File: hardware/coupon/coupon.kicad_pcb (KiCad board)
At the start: 4 copper layers, 80 x 60 mm, 78 parts, among them SW1 tactile

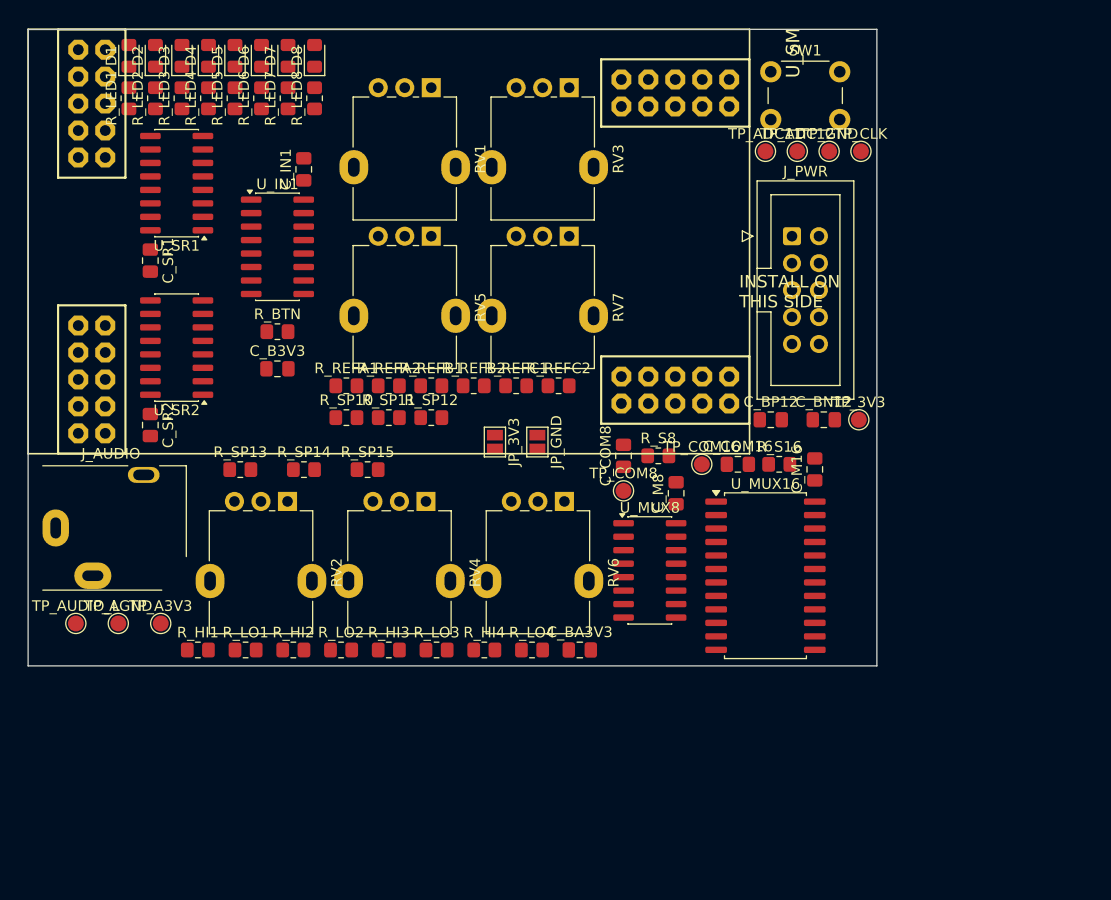
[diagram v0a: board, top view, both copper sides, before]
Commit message: hw(coupon): the board grows to 100x80, and nothing hides under the module
Co-Authored-By: HAL 9000 <293417720+bea-ton-k@users.noreply.github.com>
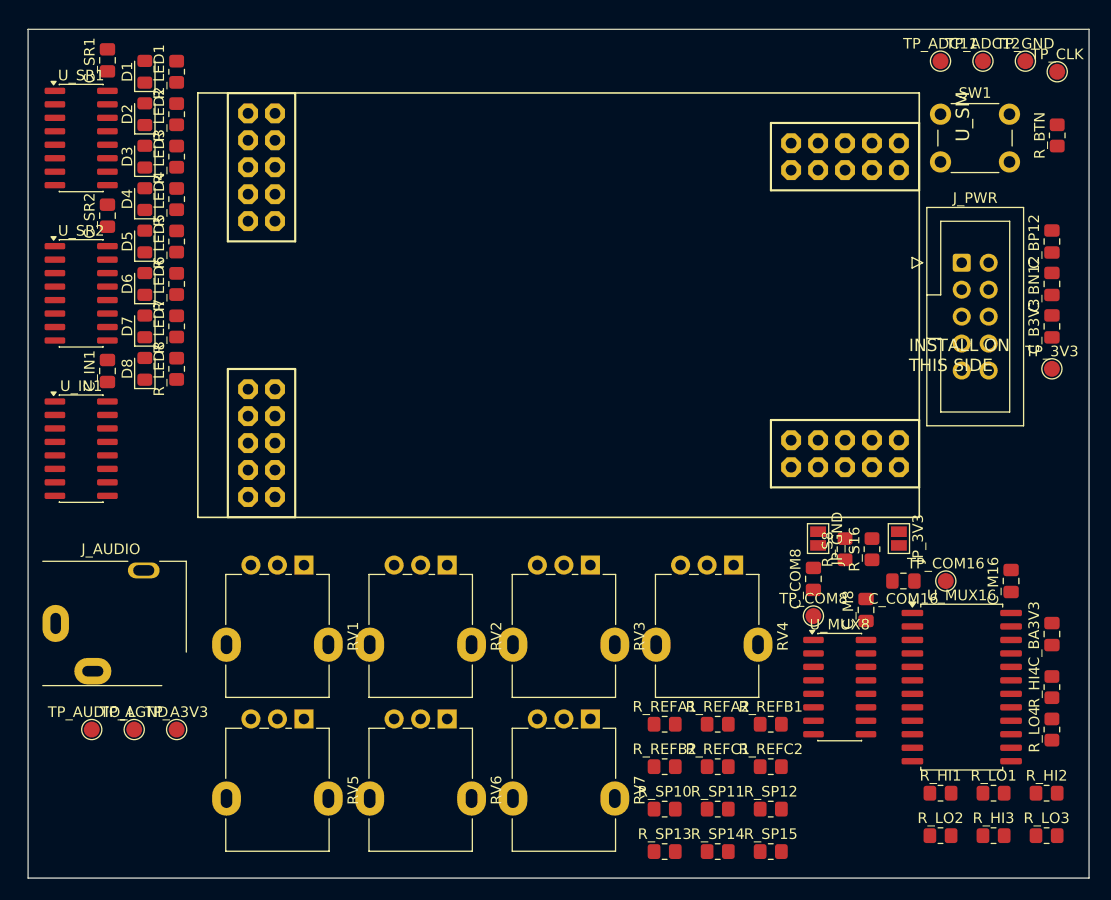
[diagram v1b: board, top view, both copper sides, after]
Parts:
- moved R_BTN 75.8 mm to (97.0, 10.0), turned to 90 degrees
- moved C_B3V3 73.1 mm to (96.5, 28.0), turned to 90 degrees
- moved R_HI2 72.3 mm to (96.0, 72.0)
- moved R_LO1 71.8 mm to (91.0, 72.0)
- moved R_HI1 71.3 mm to (86.0, 72.0)
- moved R_LO3 60.1 mm to (96.0, 76.0)
- moved R_HI3 59.6 mm to (91.0, 76.0)
- moved R_LO2 59.1 mm to (86.0, 76.0)
- moved R_SP13 53.8 mm to (60.0, 77.5)
- moved R_HI4 53.6 mm to (96.5, 62.0), turned to 90 degrees
- moved R_SP14 53.1 mm to (65.0, 77.5)
- moved R_SP15 52.3 mm to (70.0, 77.5)
- moved R_LO4 49.6 mm to (96.5, 66.0), turned to 90 degrees
- moved R_SP12 48.8 mm to (70.0, 73.5)
- moved R_SP11 48.2 mm to (65.0, 73.5)
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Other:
- board size 80 x 60 mm -> 100 x 80 mm

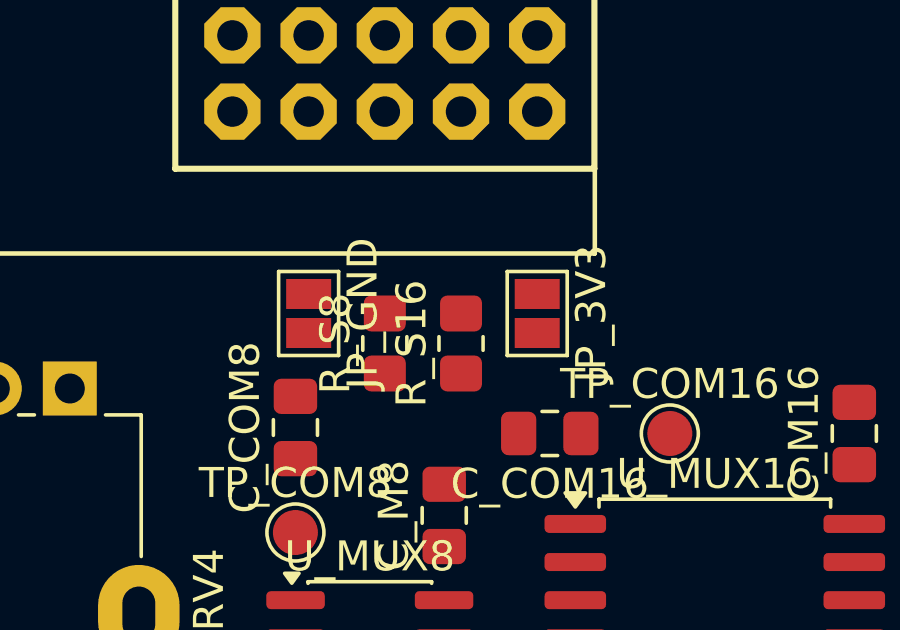
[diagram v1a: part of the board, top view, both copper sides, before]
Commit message: hw(coupon): the courtyard gate learns to fail, and to see the module
Co-Authored-By: HAL 9000 <293417720+bea-ton-k@users.noreply.github.com>
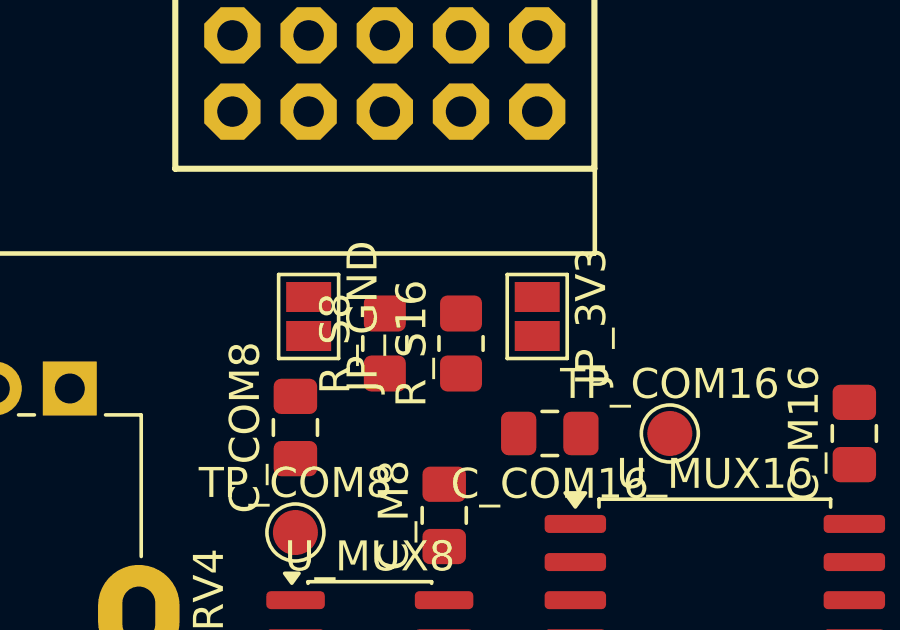
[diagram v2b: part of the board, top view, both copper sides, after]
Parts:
- moved JP_3V3 0.10 mm to (82.1, 48.1)
- moved JP_GND 0.10 mm to (74.5, 48.1)

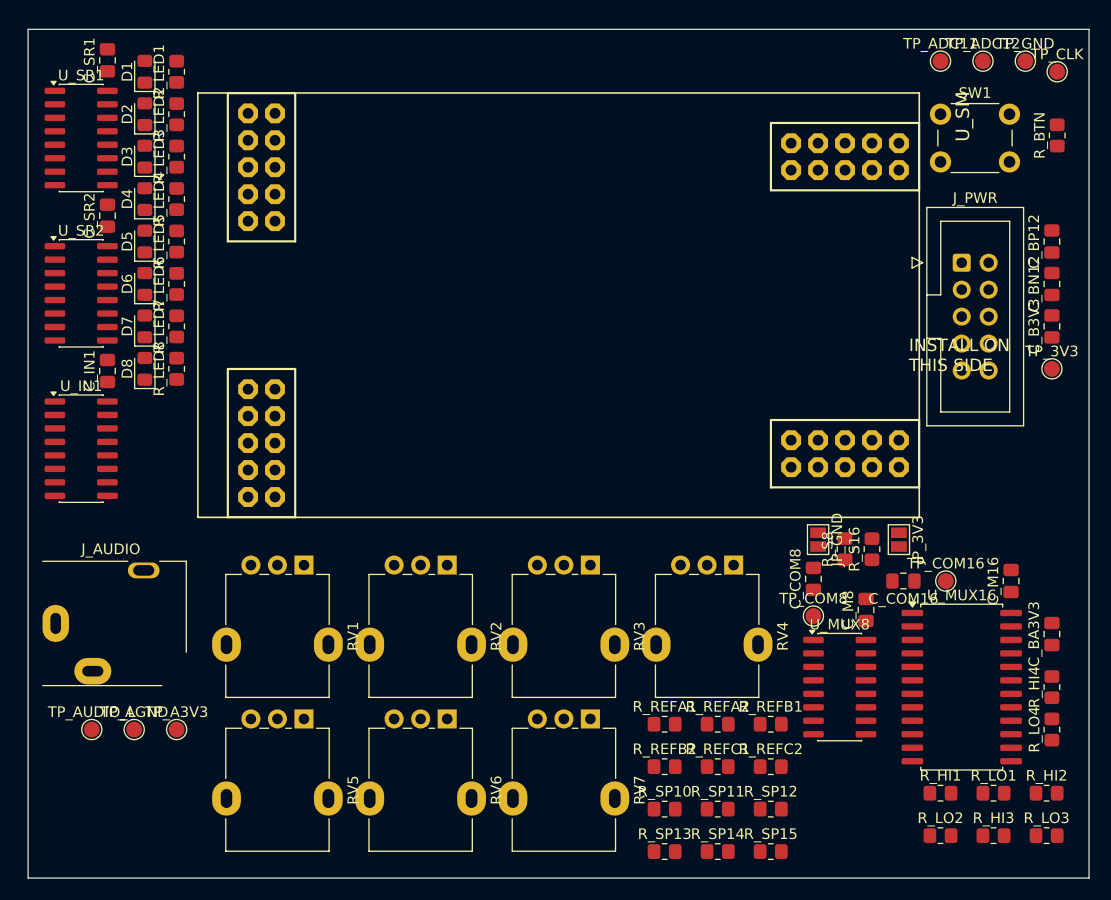
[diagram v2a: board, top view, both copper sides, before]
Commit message: hw(coupon): four split planes, joined only where the jumpers say
Zones from placement.ZONE_RECTS plus one stitching via + 0.5 mm F.Cu track
per SMD pad on a plane net, generated mechanically from the board's own
pads (through-hole plane pads reach In1/In2 through their own holes and
need nothing). Proof step 5 checks every pad on GND/AGND/+3V3/A+3V3 is
actually joined to its plane.

CONNECTIVITY_DATA's Python bindings can't answer that per-net question
directly here (GetNetItems/RunOnUnconnectedEdges both raise TypeError on
the std::vector<KICAD_T>/std::function typemaps; IsConnectedOnLayer answers
a different question and stays False for a pad stitched in one layer away)
-- probed and recorded in build_pcb.py, so the check re-parses kicad-cli's
own DRC report instead, the same trust-kicad-cli choice check_courtyards
already makes for courtyard overlaps.

The via direction took two failed attempts before landing on courtyard-
normalized axis selection: the raw pad-to-footprint-centre vector, and then
raw-magnitude axis snapping, both walked a stitching via on a two-row IC
straight into the neighbouring pin's pad -- a real shorting_items DRC
violation both times. Normalizing each axis by the footprint's own
courtyard half-extent fixed it; zero shorts in the final report.

Co-Authored-By: HAL 9000 <293417720+bea-ton-k@users.noreply.github.com>
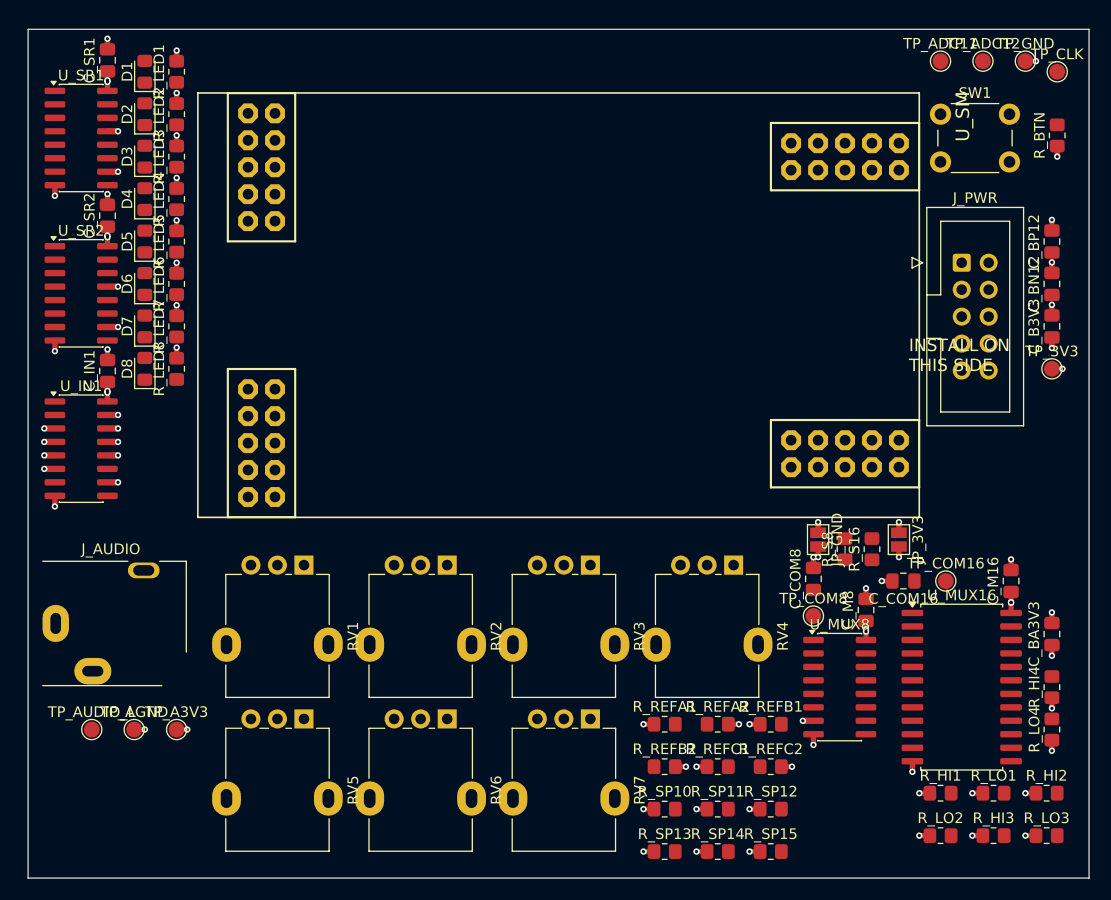
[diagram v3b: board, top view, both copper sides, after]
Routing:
- net GND: track 0.00 -> 30.0 mm, vias 0 -> 30
- net AGND: track 0.00 -> 23.0 mm, vias 0 -> 23
- net A+3V3: track 0.00 -> 14.0 mm, vias 0 -> 14
- net +3V3: track 0.00 -> 12.0 mm, vias 0 -> 12
- added copper zone on In2.Cu, net +3V3
- added copper zone on In2.Cu, net A+3V3
- added copper zone on In1.Cu, net AGND
- added copper zone on In1.Cu, net GND

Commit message: hw(coupon): the stitch search earns its own gate, and stops guessing once
Review round 1: check_courtyards only ever gated courtyards_overlap, so the
"zero shorting_items" the Task-3 report claimed was verified once and
enforced never. Add check_stitch_hygiene as proof step 6, hard-gating
shorting_items/clearance/hole_clearance/hole_to_hole at zero against the
same DRC report -- all four were genuinely zero in the Task-2 baseline, so
this is a real regression boundary. Proved red with a scratchpad-only
perturbation (a GND via dropped 0.05 mm from a +12V pad); no repo file
touched, confirmed by git status immediately after.

Replace the single-guess via placement with _find_via_offset(), a real
collision search: same courtyard-normalized starting direction, then the
perpendicular axis, then both reversed, at growing standoff up to 3.0 mm,
checked against every other-net pad's actual bounding box and every via
already placed this pass. Clears both severe cases review round 1 named
(the C_BP12/C_BN12 +-12V-adjacent via at 0.0375 mm actual clearance, and
the LED-column squeezes at ~0.10-0.15 mm) plus the via-born hole_to_hole
pairs -- all 79 stitched pads resolve on the first search, nothing left to
adjudicate. placement.py untouched; the fix only changes where within its
search radius a via lands.

Co-Authored-By: HAL 9000 <293417720+bea-ton-k@users.noreply.github.com>
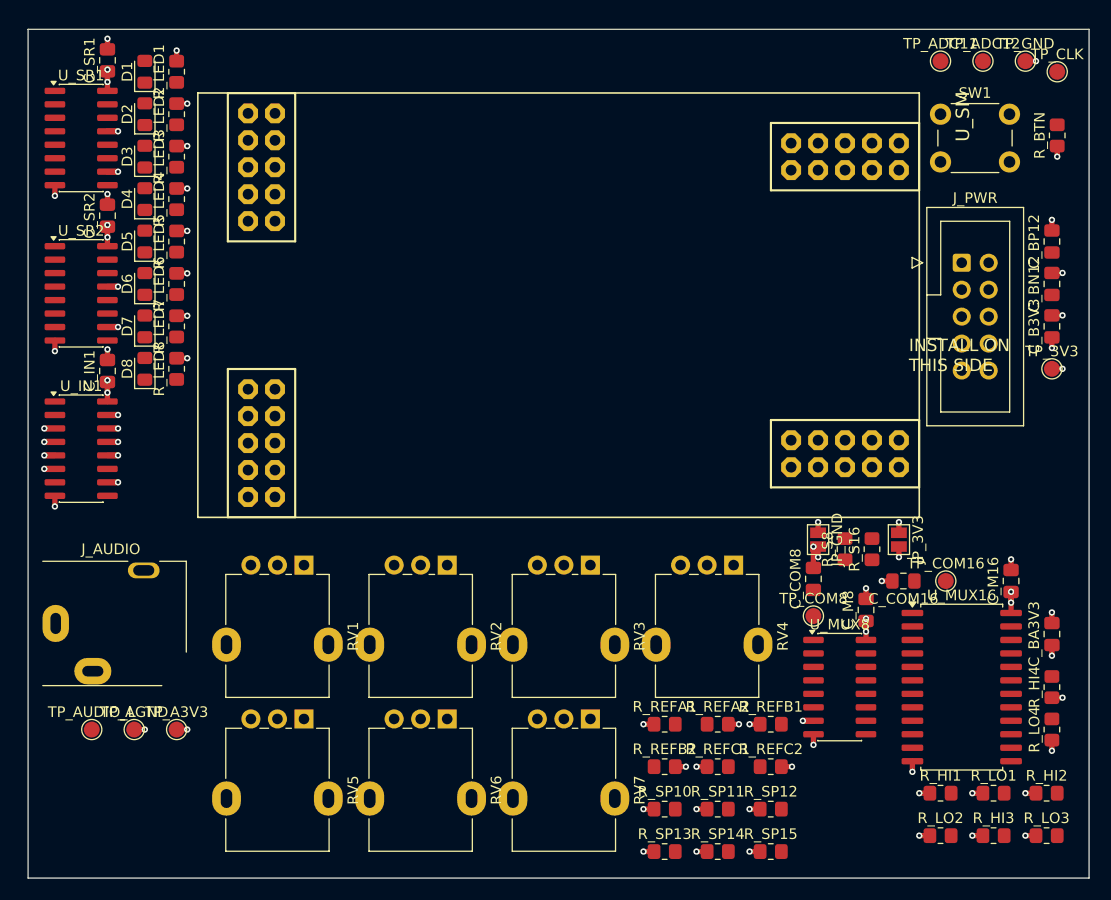
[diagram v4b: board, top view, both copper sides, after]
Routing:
- net +3V3: track 12.0 -> 15.0 mm
- net A+3V3: track 14.0 -> 16.0 mm
- net AGND: track 23.0 -> 24.0 mm

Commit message: hw(coupon): the routing is data, and the ratsnest is down to ten
74 of the board's 84 unconnected pairs are copper now, and every other gate
is green -- including tracks_crossing, which this commit adds to the DRC
classes build_pcb.py refuses to pass. It earned that on the first routing
round: the opening +-12 V draft crossed -12 V over the +12 V lane and step 3
was still filing that class under "not gated here". Fifteen further crossings
turned up behind it, every one a short.

routing.py is data and a resolver, not a router. Endpoints are named
("pad", "U_SM", "A5") and resolved from the built board, so moving a part in
placement.py moves the track's end with it. The corners in between are
hand-placed, and the reasons are written down beside them, because the
numbers that decide this layout are not visible from the source: the module's
landing pads leave 0.66 mm between neighbours against the 0.65 mm a 0.25 mm
track needs, so nothing threads a bank; an SOIC-16 leaves 0.67 mm against the
same 0.65 mm, so seven of the eight LED anodes go under the board; and Task
3's stitching sits at 1.27 mm pitch through every corridor the analog
fan-out wanted.

Ten pairs are still open, all of them the address/enable bus landing at the
two muxes and the 8:1's two east-column ties. The blocker is an ordering
contradiction rather than a shortage of room -- the fan-out order at U_SR1's
via column and the landing order at the 16:1's pins disagree about MUX_A2 and
MUX_A3, and the 16:1's own east-column descents wall the 8:1 off from its two
far ties. Written up in full in the task report; it looks like a placement
question, and placement is not this task's to change.

Co-Authored-By: HAL 9000 <293417720+bea-ton-k@users.noreply.github.com>
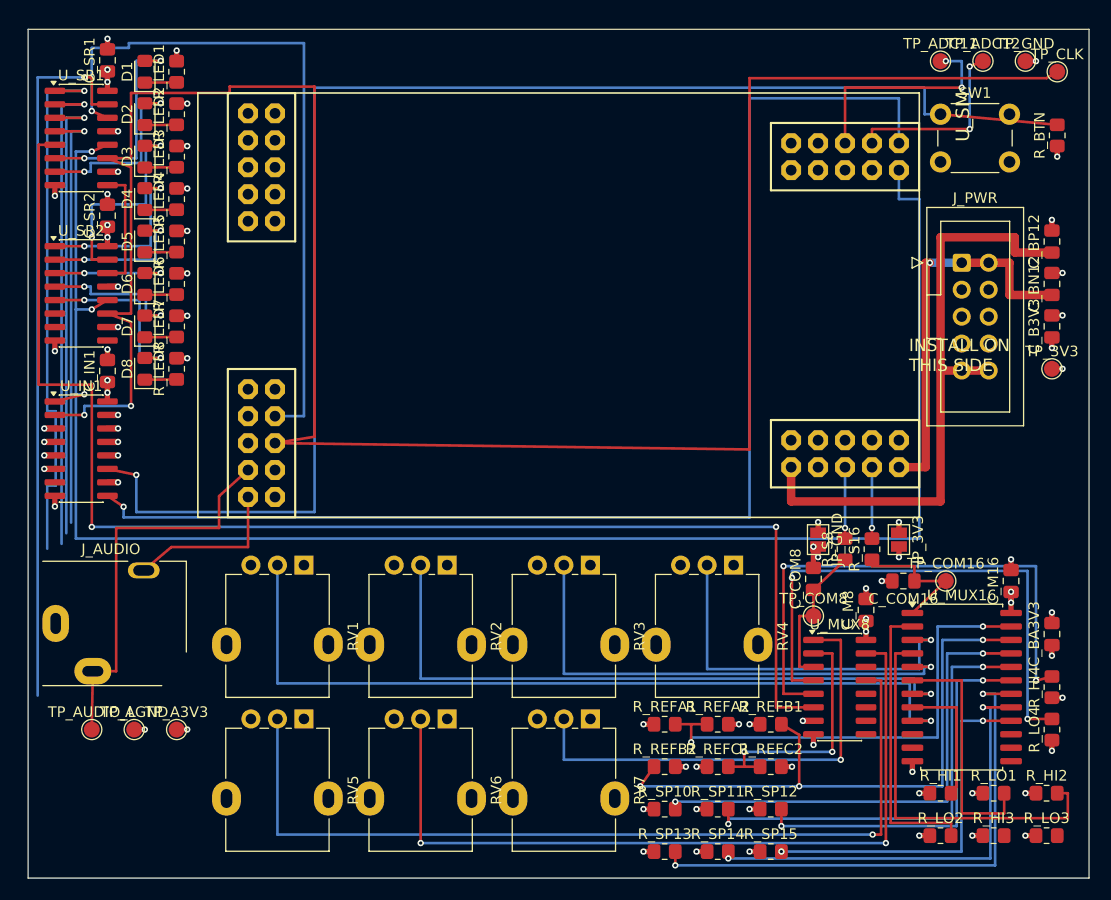
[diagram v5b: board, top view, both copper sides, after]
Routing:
- net SR_CLK: track 0.00 -> 208.6 mm, vias 0 -> 2
- net SR_LATCH: track 0.00 -> 162.6 mm, vias 0 -> 3
- net BTN_1: track 0.00 -> 135.6 mm, vias 0 -> 1
- net MUX8_EN_N: track 0.00 -> 127.6 mm, vias 0 -> 2
- net SR_DATA_IN: track 0.00 -> 119.7 mm, vias 0 -> 1
- net MUX8_CH0: track 0.00 -> 83.8 mm, vias 0 -> 1
- net MUX16_CH0: track 0.00 -> 78.0 mm, vias 0 -> 1
- net MUX8_CH2: track 0.00 -> 75.3 mm, vias 0 -> 2
- net MUX_A0: track 0.00 -> 67.4 mm, vias 0 -> 1
- net SR_DATA_OUT: track 0.00 -> 65.9 mm, vias 0 -> 1
- net MUX16_CH2: track 0.00 -> 62.0 mm, vias 0 -> 1
- net +12V: track 0.00 -> 58.7 mm
- net MUX16_CH9: track 0.00 -> 57.8 mm, vias 0 -> 3
- net MUX16_CH13: track 0.00 -> 51.4 mm, vias 0 -> 2
- net MUX_A1: track 0.00 -> 51.0 mm, vias 0 -> 1
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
